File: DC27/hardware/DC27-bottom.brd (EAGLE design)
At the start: 102.4 x 117.6 mm, 87 parts, among them IC2 LDL112D33R, IC3 FT2232HL-REEL, IC4 93LC46BT-I_OT, J1 PAIRING, J2 JTAG, J3 Battery, J4 Program Port, U2 ESP-WROOM-32, Y1 ABM7-12.000MHZ-D2Y-T

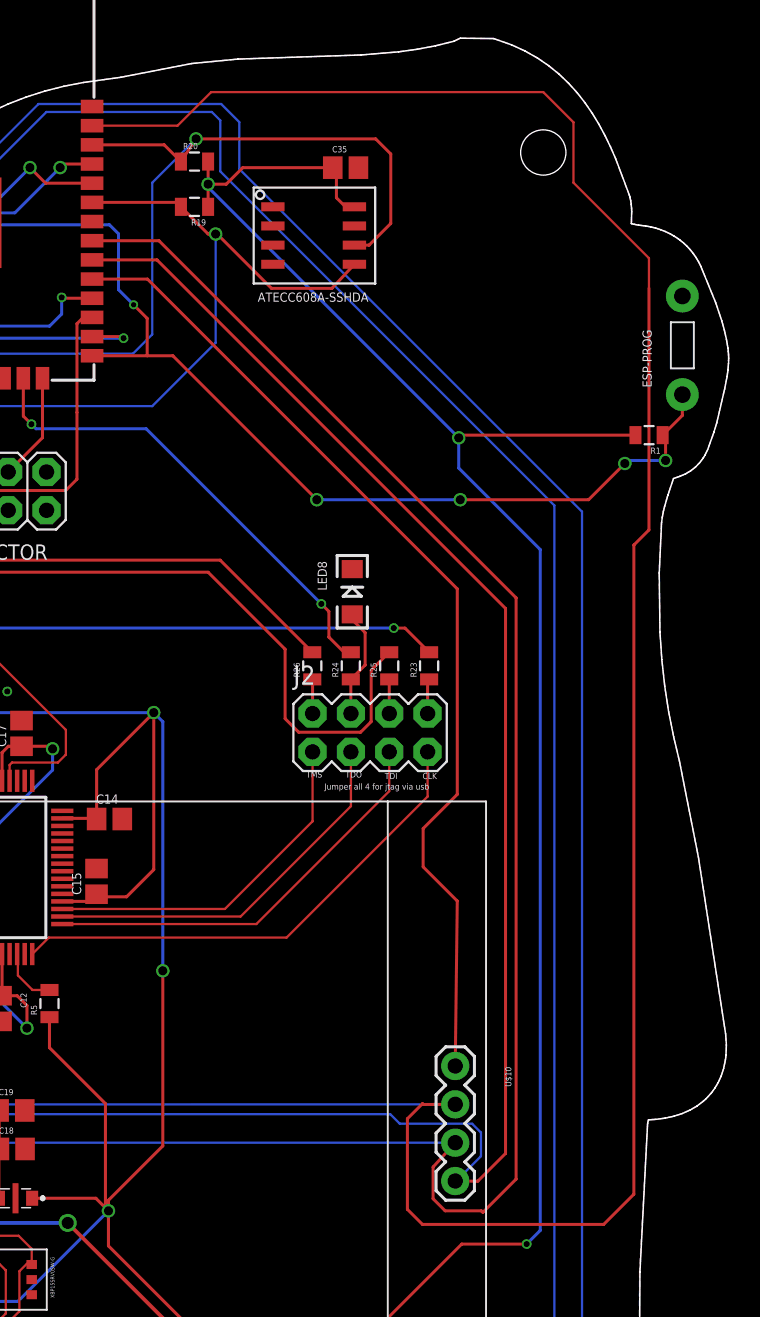
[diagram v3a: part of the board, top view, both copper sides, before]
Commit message: tweaked position of the led 7 and 8 to be at same Y as the right eye (+/- .1 mm) rerouted trace so it does not go between resistor on bottom board
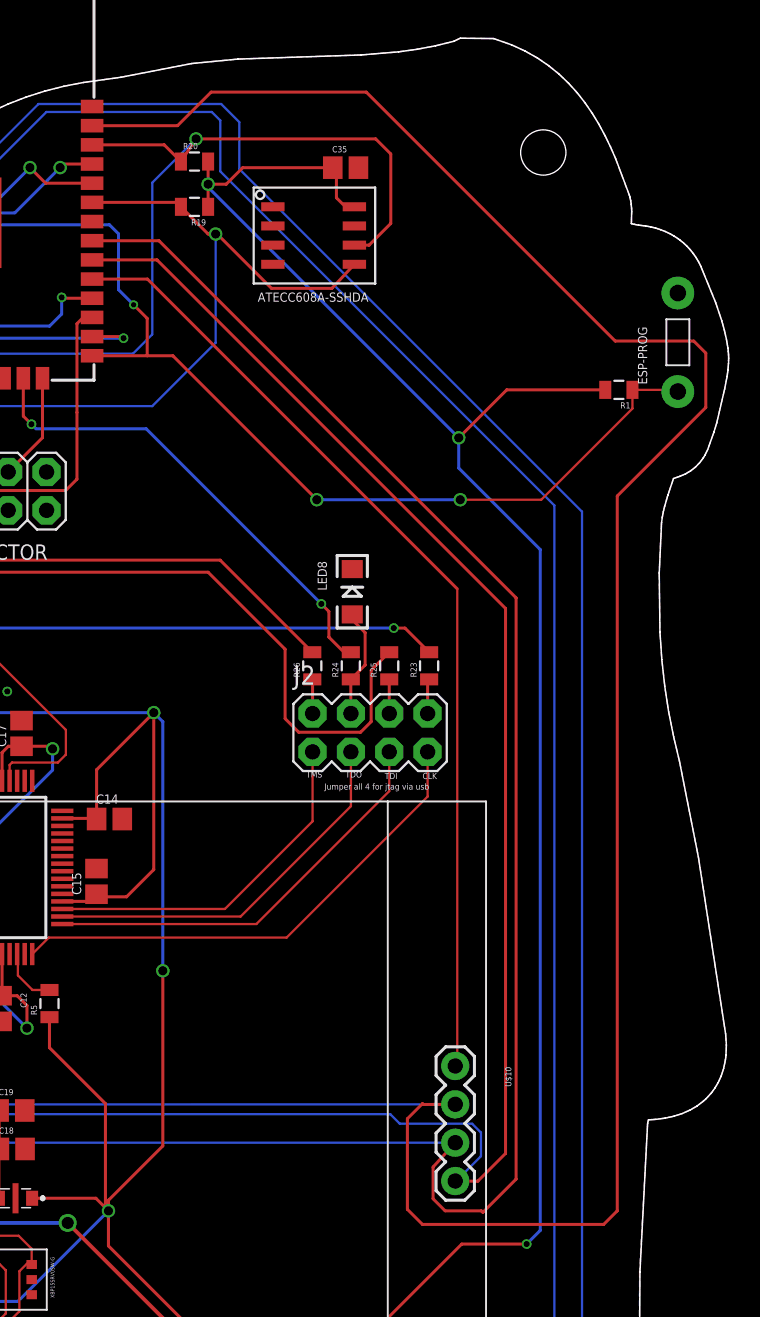
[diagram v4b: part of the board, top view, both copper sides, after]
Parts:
- moved R1 3.61 mm to (95.1, 94.3)
- moved ESP-PROG 0.36 mm to (99.0, 97.4)
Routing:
- net SD_CS: track 66.2 -> 64.3 mm
- net ESP-IO0: track 121.7 -> 120.2 mm, vias 5 -> 3
- net VCC: track 620.8 -> 620.1 mm
- net DISPLAY_SD_MOSI: track 207.1 -> 206.4 mm
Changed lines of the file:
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@@
 <attribute name="NAME" x="2.712628125" y="94.771859375" size="0.6096" layer="25" font="vector" ratio="10" rot="R90"/>
 </element>
-<element name="ESP-PROG" library="dc-26" package="TACTILE-2PIN-NARROW" value="UserButton" x="99.346228125" y="97.217059375" smashed="yes" rot="R90">
-<attribute name="NAME" x="97.314228125" y="94.423059375" size="0.6096" layer="25" font="vector" ratio="10" rot="R90"/>
-</element>
-<element name="R1" library="dc-26" package="0805" value="10 K" x="97.141028125" y="91.266659375" smashed="yes" rot="R180">
-<attribute name="NAME" x="97.903028125" y="90.441159375" size="0.4064" layer="25" rot="R180"/>
+<element name="ESP-PROG" library="dc-26" package="TACTILE-2PIN-NARROW" value="UserButton" x="99.046228125" y="97.417059375" smashed="yes" rot="R90">
+<attribute name="NAME" x="97.014228125" y="94.623059375" size="0.6096" layer="25" font="vector" ratio="10" rot="R90"/>
+</element>
+<element name="R1" library="dc-26" package="0805" value="10 K" x="95.141028125" y="94.266659375" smashed="yes" rot="R180">
+<attribute name="NAME" x="95.903028125" y="93.441159375" size="0.4064" layer="25" rot="R180"/>
 </element>
 <element name="R4" library="dc-26" package="0805" value="10 K" x="6.910228125" y="92.027459375" smashed="yes" rot="R270">
@@
 </element>
 <element name="TOP-BOT-CONNECTOR" library="connector" package="2X6" value="M06X2" x="44.534228125" y="86.289059375" smashed="yes">
-<attribute name="NAME" x="43.244228125" y="83.014059375" size="1.016" layer="25" ratio="10"/>
+<attribute name="NAME" x="43.244228125" y="83.014059375" size="1.016" layer="25" font="vector" ratio="10"/>
 </element>
 <element name="PWR" library="switches" package="MSS3VTR" value="MSS3-V-T_R" x="71.2" y="10.4" smashed="yes" rot="R324">
@@
 <wire x1="77.030228125" y1="106.393059375" x2="77.624228125" y2="106.393059375" width="0.2" layer="1"/>
 <via x="84.534228125" y="91.089059375" extent="1-16" drill="0.6"/>
-<wire x1="96.241028125" y1="91.266659375" x2="84.711828125" y2="91.266659375" width="0.2" layer="1"/>
-<wire x1="84.711828125" y1="91.266659375" x2="84.534228125" y2="91.089059375" width="0.2" layer="1"/>
+<wire x1="94.241028125" y1="94.266659375" x2="87.711828125" y2="94.266659375" width="0.2" layer="1"/>
+<wire x1="87.711828125" y1="94.266659375" x2="84.534228125" y2="91.089059375" width="0.2" layer="1"/>
 <wire x1="67.934228125" y1="107.889059375" x2="67.934228125" y2="107.689059375" width="0.2" layer="16"/>
 <wire x1="84.534228125" y1="91.089059375" x2="67.934228125" y2="107.689059375" width="0.2" layer="16"/>
@@
 <contactref element="U2" pad="29"/>
 <contactref element="U$10" pad="15"/>
-<wire x1="82.176828125" y1="62.672096875" x2="82.176828125" y2="65.213221875" width="0.2" layer="1"/>
-<wire x1="84.3036" y1="49.4836" x2="84.437828125" y2="60.411096875" width="0.2" layer="1"/>
-<wire x1="84.437828125" y1="67.474221875" x2="84.437828125" y2="81.085459375" width="0.2" layer="1"/>
-<wire x1="84.437828125" y1="60.411096875" x2="82.176828125" y2="62.672096875" width="0.2" layer="1"/>
-<wire x1="82.176828125" y1="65.213221875" x2="84.437828125" y2="67.474221875" width="0.2" layer="1"/>
 <wire x1="63.918228125" y1="101.605059375" x2="60.250228125" y2="101.605059375" width="0.2" layer="1"/>
 <wire x1="84.437828125" y1="81.085459375" x2="63.918228125" y2="101.605059375" width="0.2" layer="1"/>
+<wire x1="84.3036" y1="49.4836" x2="84.437828125" y2="49.617828125" width="0.1524" layer="1"/>
+<wire x1="84.437828125" y1="81.085459375" x2="84.437828125" y2="49.617828125" width="0.1524" layer="1"/>
 </signal>
 <signal name="DISPLAY_SD_MISO">
@@
 <contactref element="U2" pad="25"/>
 <contactref element="ESP-PROG" pad="P$2"/>
-<wire x1="98.041028125" y1="91.266659375" x2="99.346228125" y2="92.571859375" width="0.2" layer="1"/>
-<wire x1="99.346228125" y1="92.571859375" x2="99.346228125" y2="93.953159375" width="0.2" layer="1"/>
 <wire x1="60.250228125" y1="96.525059375" x2="63.9" y2="96.525059375" width="0.2" layer="1"/>
 <wire x1="63.9" y1="96.525059375" x2="65.598228125" y2="96.525059375" width="0.2" layer="1"/>
@@
 <wire x1="75.134228125" y1="86.989059375" x2="84.634228125" y2="86.989059375" width="0.2" layer="16"/>
 <via x="84.634228125" y="86.989059375" extent="1-16" drill="0.6"/>
-<wire x1="98.041028125" y1="91.266659375" x2="98.234228125" y2="91.073459375" width="0.2" layer="1"/>
-<wire x1="98.234228125" y1="91.073459375" x2="98.234228125" y2="89.589059375" width="0.2" layer="1"/>
-<via x="98.234228125" y="89.589059375" extent="1-16" drill="0.6"/>
-<wire x1="98.234228125" y1="89.589059375" x2="95.734228125" y2="89.589059375" width="0.2" layer="16"/>
-<wire x1="95.734228125" y1="89.589059375" x2="95.534228125" y2="89.389059375" width="0.2" layer="16"/>
-<via x="95.534228125" y="89.389059375" extent="1-16" drill="0.6"/>
-<wire x1="95.534228125" y1="89.389059375" x2="93.134228125" y2="86.989059375" width="0.2" layer="1"/>
-<wire x1="93.134228125" y1="86.989059375" x2="84.634228125" y2="86.989059375" width="0.2" layer="1"/>
 <contactref element="J4" pad="3"/>
 <wire x1="11.5276" y1="90.58545" x2="11.87545" y2="90.2376" width="0.2" layer="16"/>
@@
 <wire x1="63.9" y1="99" x2="63.9" y2="96.525059375" width="0.2" layer="1"/>
 <wire x1="62" y1="104.6" x2="62" y2="100.9" width="0.2" layer="16"/>
+<wire x1="90" y1="86.989059375" x2="84.634228125" y2="86.989059375" width="0.1524" layer="1"/>
+<wire x1="96.041028125" y1="94.266659375" x2="98.932728125" y2="94.266659375" width="0.1524" layer="1"/>
+<wire x1="98.932728125" y1="94.266659375" x2="99.046228125" y2="94.153159375" width="0.1524" layer="1"/>
+<wire x1="96.041028125" y1="94.266659375" x2="96.041028125" y2="93.0300875" width="0.1524" layer="1"/>
+<wire x1="96.041028125" y1="93.0300875" x2="90" y2="86.989059375" width="0.1524" layer="1"/>
 </signal>
 <signal name="DISPLAY_SD_MOSI">
@@
 <wire x1="81.134228125" y1="39.989059375" x2="82.134228125" y2="38.989059375" width="0.2" layer="1"/>
 <wire x1="82.134228125" y1="38.989059375" x2="94.134228125" y2="38.989059375" width="0.2" layer="1"/>
-<wire x1="94.134228125" y1="38.989059375" x2="96.134228125" y2="40.989059375" width="0.2" layer="1"/>
-<wire x1="96.134228125" y1="40.989059375" x2="96.134228125" y2="83.989059375" width="0.2" layer="1"/>
-<wire x1="96.134228125" y1="83.989059375" x2="97.134228125" y2="84.989059375" width="0.2" layer="1"/>
-<wire x1="97.134228125" y1="84.989059375" x2="97.134228125" y2="100.989059375" width="0.2" layer="1"/>
-<wire x1="97.134228125" y1="100.989059375" x2="97.134228125" y2="102.989059375" width="0.1524" layer="1"/>
-<wire x1="97.134228125" y1="102.989059375" x2="92.134228125" y2="107.989059375" width="0.1524" layer="1"/>
-<wire x1="92.134228125" y1="107.989059375" x2="92.134228125" y2="111.989059375" width="0.1524" layer="1"/>
-<wire x1="92.134228125" y1="111.989059375" x2="90.134228125" y2="113.989059375" width="0.1524" layer="1"/>
-<wire x1="90.134228125" y1="113.989059375" x2="68.134228125" y2="113.989059375" width="0.1524" layer="1"/>
-<wire x1="68.134228125" y1="113.989059375" x2="65.910228125" y2="111.765059375" width="0.1524" layer="1"/>
-<wire x1="65.910228125" y1="111.765059375" x2="60.250228125" y2="111.765059375" width="0.1524" layer="1"/>
+<wire x1="94.134228125" y1="38.989059375" x2="95.034228125" y2="39.889059375" width="0.2" layer="1"/>
+<wire x1="95.034228125" y1="39.889059375" x2="95.034228125" y2="87.234228125" width="0.2" layer="1"/>
+<wire x1="94.9" y1="97.5" x2="78.410940625" y2="113.989059375" width="0.2" layer="1"/>
+<wire x1="78.410940625" y1="113.989059375" x2="68.134228125" y2="113.989059375" width="0.2" layer="1"/>
+<wire x1="68.134228125" y1="113.989059375" x2="65.910228125" y2="111.765059375" width="0.2" layer="1"/>
+<wire x1="65.910228125" y1="111.765059375" x2="60.250228125" y2="111.765059375" width="0.2" layer="1"/>
+<wire x1="100.9" y1="93.1" x2="100.9" y2="96.7" width="0.2" layer="1"/>
+<wire x1="100.9" y1="96.7" x2="100.1" y2="97.5" width="0.2" layer="1"/>
+<wire x1="100.1" y1="97.5" x2="94.9" y2="97.5" width="0.2" layer="1"/>
+<wire x1="95.034228125" y1="87.234228125" x2="100.9" y2="93.1" width="0.2" layer="1"/>
 </signal>
 <signal name="JTAG_TDO_LED1">
